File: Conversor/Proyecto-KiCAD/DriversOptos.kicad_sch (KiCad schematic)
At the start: 35 parts, among them U10 ACPL-P480, U11 ACPL-P480, U12 2ED21834-S06J, U13 2ED21834-S06J, U8 ACPL-P480, U9 ACPL-P480

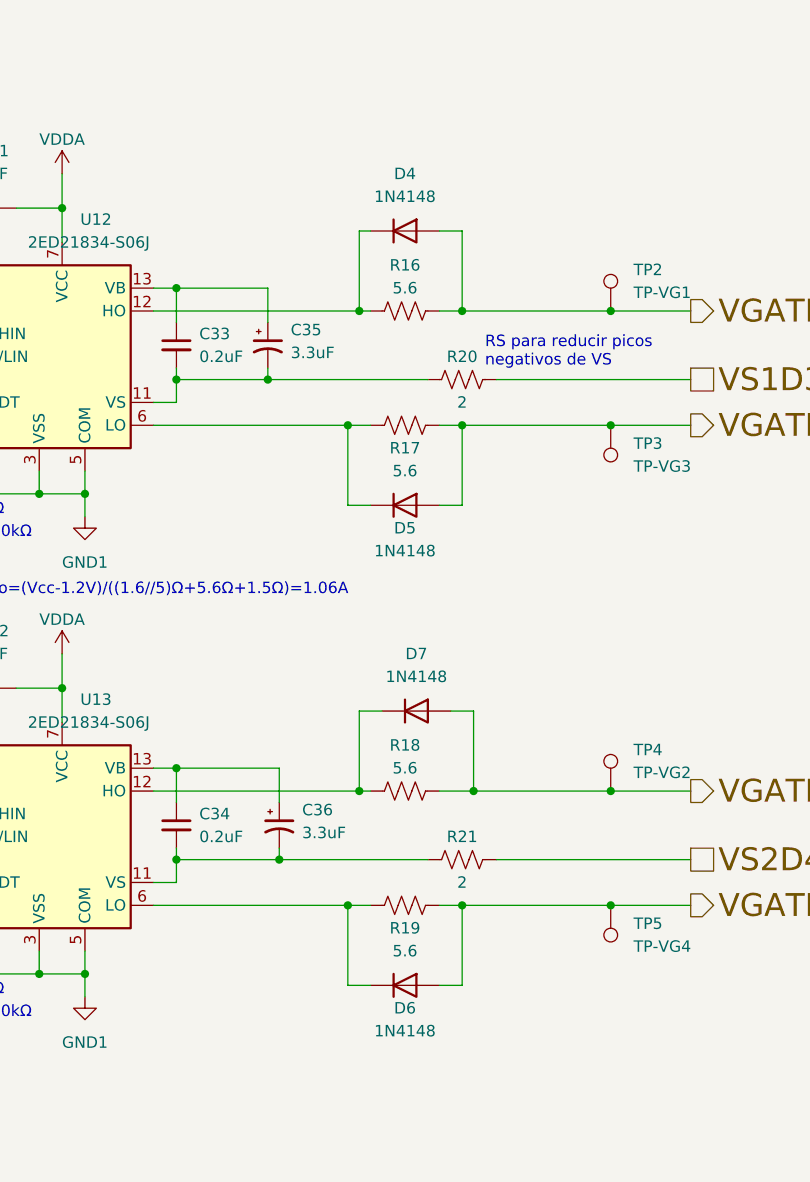
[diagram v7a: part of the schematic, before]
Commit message: Finalizar la PCB y mandarla a fabricar
- Agregar cambios sugeridos por Jorge el 2022/07/22
- Bloqueados todos los componentes de la PCB (no modificar más)
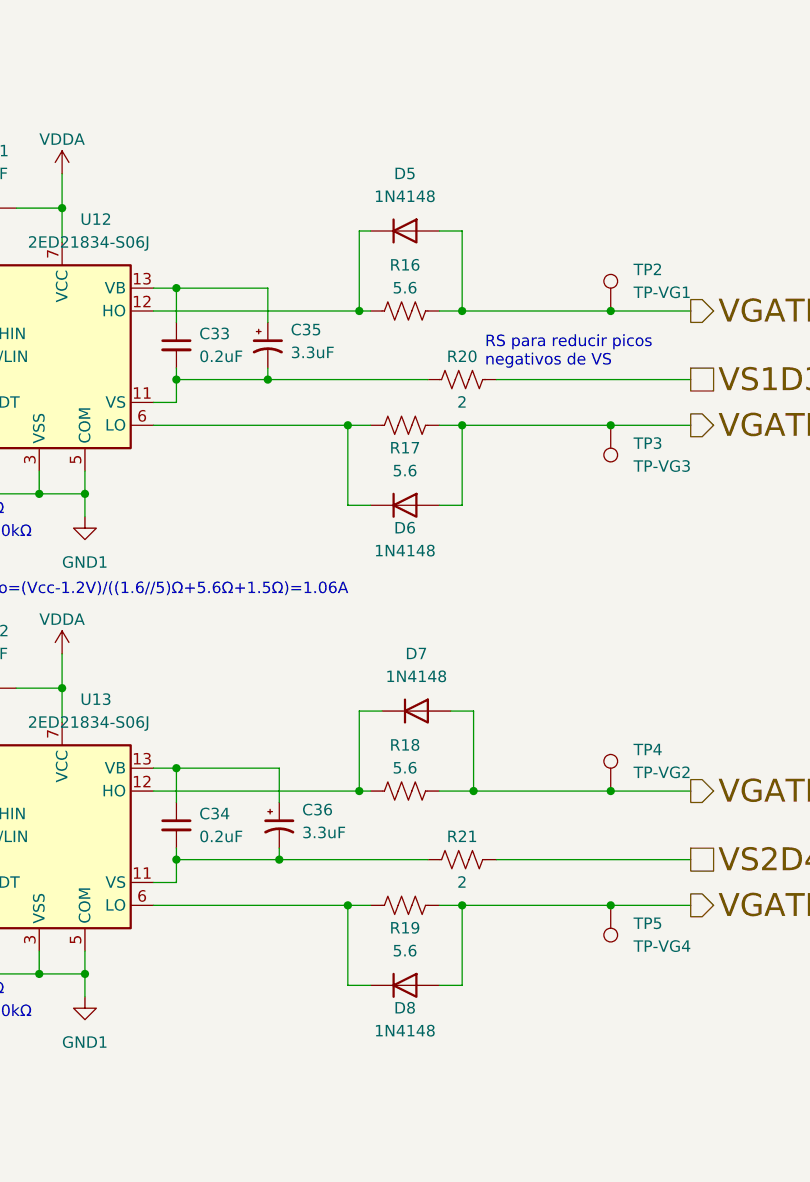
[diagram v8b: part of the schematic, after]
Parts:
- renumbered D4 to D5, D5 to D6, D6 to D8
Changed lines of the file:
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@@
   (symbol (lib_id "Diode:1N4148") (at 229.87 54.61 0) (unit 1)
     (in_bom yes) (on_board yes) (fields_autoplaced)
-    (property "Reference" "D4" (id 0) (at 229.87 48.26 0))
+    (property "Reference" "D5" (id 0) (at 229.87 48.26 0))
     (property "Value" "1N4148" (id 1) (at 229.87 50.8 0))
     (property "Footprint" "Diode_THT:D_DO-35_SOD27_P7.62mm_Horizontal" (id 2) (at 229.87 59.055 0)
@@
   (symbol (lib_id "Diode:1N4148") (at 229.87 138.43 0) (unit 1)
     (in_bom yes) (on_board yes)
-    (property "Reference" "D6" (id 0) (at 229.87 140.97 0))
+    (property "Reference" "D8" (id 0) (at 229.87 140.97 0))
     (property "Value" "1N4148" (id 1) (at 229.87 143.51 0))
     (property "Footprint" "Diode_THT:D_DO-35_SOD27_P7.62mm_Horizontal" (id 2) (at 229.87 142.875 0)
@@
   (symbol (lib_id "Diode:1N4148") (at 229.87 85.09 0) (unit 1)
     (in_bom yes) (on_board yes)
-    (property "Reference" "D5" (id 0) (at 229.87 87.63 0))
+    (property "Reference" "D6" (id 0) (at 229.87 87.63 0))
     (property "Value" "1N4148" (id 1) (at 229.87 90.17 0))
     (property "Footprint" "Diode_THT:D_DO-35_SOD27_P7.62mm_Horizontal" (id 2) (at 229.87 89.535 0)
